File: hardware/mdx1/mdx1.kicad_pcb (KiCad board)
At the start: 4 copper layers, 135 x 92 mm, 322 parts, among them J1 USB-C 16P, J2 USBLC6-2SC6 (USB ESD), J3 Battery JST-PH 3p, J4 Coil header 1x06 2.54mm, J5 SWD 10p 1.27mm, J6 microSD (Hirose DM3AT), J7 UI link FFC 20p 0.5mm, J8 3.5 mm jack, J9 Speaker 8R, Q1 SiR626DP (60V), Q2 BSC190N15NS3 (150V), Q3 BSS127S (600V), Q4 BSC320N20NS3 G, Q5 BSC320N20NS3 G, Q6 BSC320N20NS3 G, Q7 BSC320N20NS3 G, Q8 2N7002, U1 BQ24075RGT, U10 UCC27714D, U11 UCC27714D, U12 INA241A2 (20 V/V), U13 TLV3501 4.5 V (+5 A), U14 TLV3501 0.5 V (-5 A), U15 OPA1612, U16 THS4551 (G=1), U17 THS4551 (G=1), U18 OPA1656, U19 ADS127L01 (ch A), U2 BQ27441-G1A, U20 ADS127L01 (ch B), U21 REF5025 (2.500 V, 3 ppm/C), U22 STM32H743ZIT6, U23 LSM6DSM (IMU), U24 TPA6132A2 (HP amp), U25 PAM8302A (2.5 W class-D), U26 BM83SM1-00AA, U27 MAX-M10S (GNSS), U28 GNSS chip antenna, U3 TPS63001 (3.3V), U4 TPS65131RGE, U5 LT3045 (+5VA), U6 LT3094 (-5VA), U7 TPS7A2033 (+3V3A), U8 LT3757 (VTX 8-30V), U9 LT3757 (VBRIDGE 100V), Y1 16.384 MHz 3225, Y2 32.768 kHz 3215

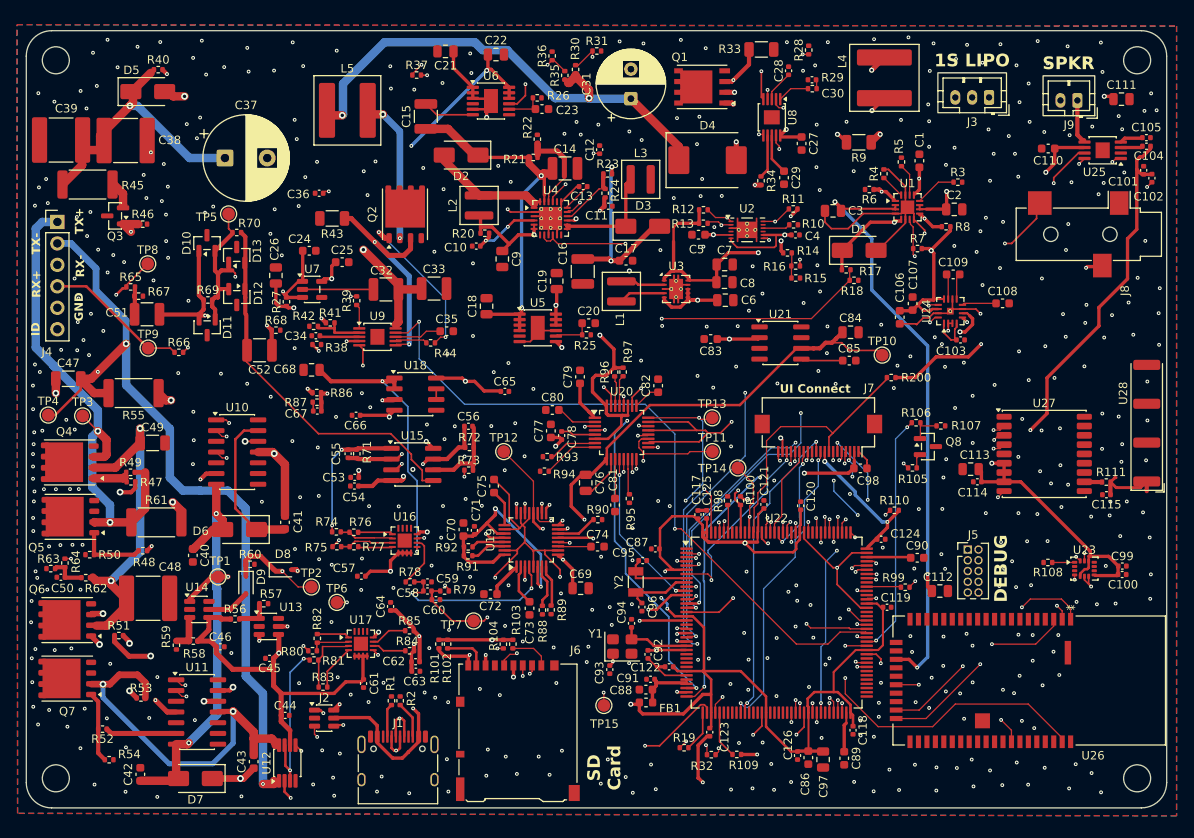
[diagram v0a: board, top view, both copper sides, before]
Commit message: Re-source out-of-stock parts; rework D8/9 footprint and GNSS antenna front end
Parts re-sourced to in-stock equivalents (BOM + board + firmware kept in sync):
- U4  TPS65131RGET, U12 INA241A2QDGKRQ1, U23 LSM6DSO32TR (same footprints)
- Q1  SiR680ADP-T1-UE3 (80 V, same PowerPAK SO-8; higher Qg - verify gate drive)
- U2  BQ27441DRZT-G1A (drop-in, R9 sense retained)
- D8/9 NSVBAT54SWT1G: SOT-323/SC-70 dual-series wired as a single diode
  (anode=pin1, cathode=pin3, pin2 NC); footprint changed on the board
- C32/C33/C38-48 re-sourced (KEMET/Murata/TDK), same footprints

GNSS antenna: chip antenna -> external active antenna via u.FL
- Removed U28 (chip antenna), C115 (match pad), R111 (0R RF series-match)
- Added J13 u.FL (Molex 73412-0110) + bias-tee: L8 27nH feed, C127 33pF DC block,
  C128 10nF VCC_RF bypass, D17 PESD0402-140 ESD (verify Vrwm >= 5 V)

Firmware:
- mdx_config.h: MDX_ITX_V_PER_A 0.4 -> 1.0 (INA241A2 is 50 V/V, not 20)
- hal_stm32.c: LSM6DSO32 accel init 0x48 -> 0x40 (FS_XL encoding differs; keeps +-4 g)
- make test: 96 checks pass

BOM: bom_data.json reconciled to the updated board (every placed part has an MPN;
fab BOM drops only the 15 test points). Regenerated JLCPCB fab package and the
DigiKey upload BOM (grouped by MPN, compact references).
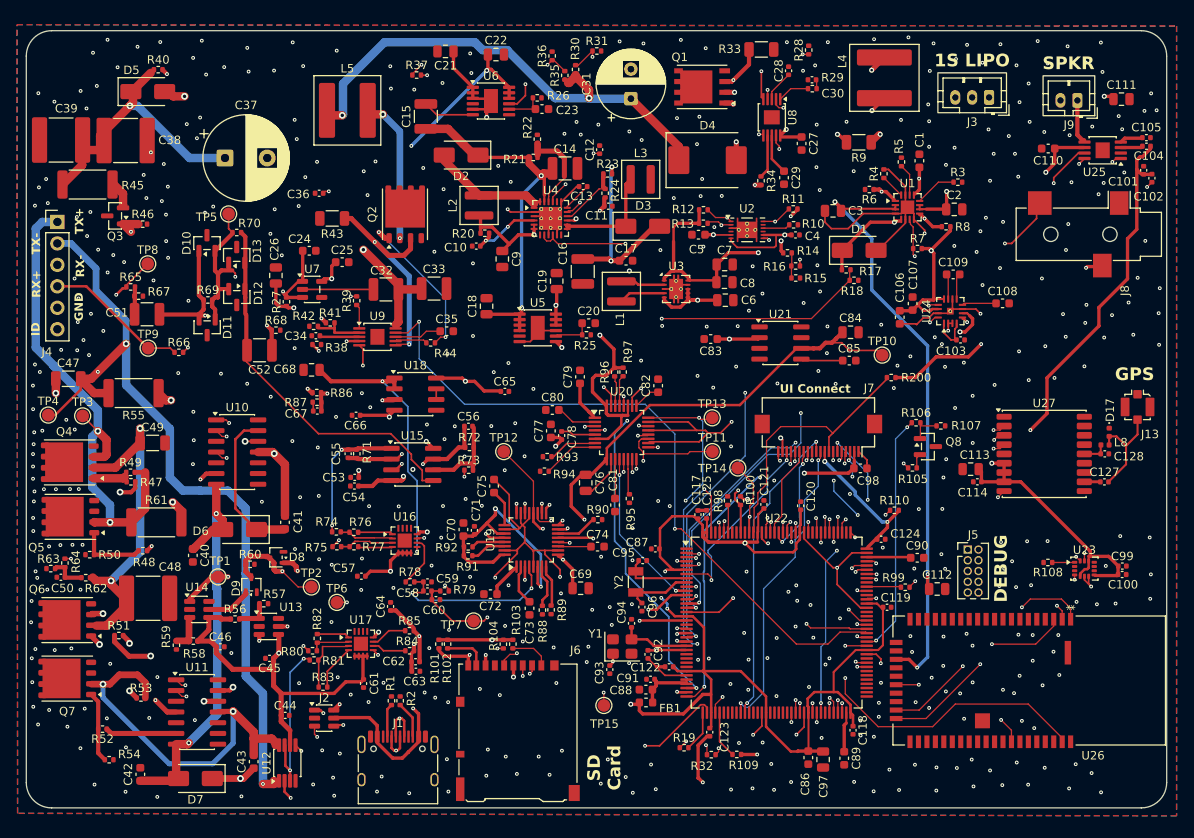
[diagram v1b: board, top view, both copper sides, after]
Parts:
- removed C115: DNP (match, shunt), Capacitor_SMD:C_0402_1005Metric
- removed C126: 100n, Capacitor_SMD:C_0402_1005Metric
- removed H1, H2, H3, H4: MountingHole_3.2mm_M3, MountingHole_3.2mm_M3
- removed R111: 0R (match, series), Resistor_SMD:R_0402_1005Metric
- removed U28: GNSS chip antenna, RF_Antenna:Antenova_SR4G013_GPS
- added C127: 33 pF, Capacitor_SMD:C_0402_1005Metric, F.Cu at (177.6, 103.4)
- added C128: 10nF, Capacitor_SMD:C_0402_1005Metric, F.Cu at (177.7, 100.1)
- added D17: PESD0402-140, Diode_SMD:D_0402_1005Metric, F.Cu at (178.2, 97.5)
- added J13: Conn_Coaxial, Connector_Coaxial:U.FL_Molex_MCRF_73412-0110_Vertical, F.Cu at (181.6, 94.5)
- added L8: 27nH, Inductor_SMD:L_0402_1005Metric, F.Cu at (177.7, 99.0)
- D8, D9: value BAT54WS -> NSVBAT54SWT1G; footprint Diode_SMD:D_SOD-323 -> Package_TO_SOT_SMD:SOT-323_SC-70
- Q1: value SiR626DP (60V) -> SiR680ADP-T1-UE3
- U12: value INA241A2 (20 V/V) -> INA241A2QDGKRQ1
- U2: value BQ27441-G1A -> BQ27441DRZT-G1A
- U23: value LSM6DSM (IMU) -> LSM6DSO32TR
- U4: value TPS65131RGE -> TPS65131RGET
- moved D8 1.67 mm to (79.6, 112.3), turned to 180 degrees
- moved D9 0.63 mm to (76.6, 115.6), turned to 90 degrees
- moved C112 0.40 mm to (157.8, 116.1)
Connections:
- D8 pad 1: TX_FAULT -> /TX driver: 3-level H-bridge, current sense, over-current trip/OC_HI
- D8 pad 2: /TX driver: 3-level H-bridge, current sense, over-current trip/OC_HI -> unconnected-(D8-K-Pad2)
- D9 pad 1: TX_FAULT -> /TX driver: 3-level H-bridge, current sense, over-current trip/OC_LO
- D9 pad 2: /TX driver: 3-level H-bridge, current sense, over-current trip/OC_LO -> unconnected-(D9-K-Pad2)
- U27 pad 11: /UI, audio, wireless: memory LCD, keypad, IMU, headphone + speaker amps, Bluetooth audio, GNSS/GNSS_RF -> Net-(U27-RF_IN)
- U27 pad 14: unconnected-(U27-VCC_RF-Pad14) -> Net-(U27-VCC_RF)
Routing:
- net Net-(D17-A2): track 0.00 -> 12.3 mm
- net /UI, audio, wireless: memory LCD, keypad, IMU, headphone + speaker amps, Bluetooth audio, GNSS/GNSS_ANT: track 6.97 -> 0.00 mm
- net Net-(U27-VCC_RF): track 0.00 -> 3.00 mm
- net /UI, audio, wireless: memory LCD, keypad, IMU, headphone + speaker amps, Bluetooth audio, GNSS/GNSS_RF: track 2.49 -> 0.00 mm
- net Net-(U27-RF_IN): track 0.00 -> 2.33 mm
- net /TX driver: 3-level H-bridge, current sense, over-current trip/OC_HI: track 8.89 -> 10.4 mm
- net TX_FAULT: track 95.4 -> 96.2 mm
- net VBAT: track 95.3 -> 94.5 mm
- net GND: vias 486 -> 461
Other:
- board text added: "GPS"

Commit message: Add LL-audio + expansion-header support (firmware, schematic nets, mount holes)
Firmware (host bench 96/0):
- Optional low-latency audio module (nRF52840 daughterboard on J14): settings
  item "Low-latency audio" + "Pair LL headphones" (auto-exposed to UI and app via
  the item table), settings_t.ll_audio, HAL hal_ll_audio_*(), USART3 (PD8/PD9) +
  PG0/PG1 on the target; BM83 kept for BLE/app + standard-BT audio. Sim stubs.
- Expansion header: I2C4 (PF14/PF15), SPI2 (PB13/14/15, CS PG8), UART5 (PB6/PB12),
  GPIO PE13/PA15 initialised; portable hal_exp_*() API + sim stubs.

Schematic: J14 LL-audio header and expansion-header nets wired to the MCU; cleared
the no-connect flags on the newly used STM32 pins (PD8/9, PG0/1, PF14/15, PB13/14/15,
PG8, PB6, PB12, PE13, PA15).

Board: added 4x M3 (3.2 mm) mounting holes (H1-H4) to the main board at the
enclosure positions (128 x 85 mm rectangle, 3.55 mm inset).

Docs: firmware guide menu, design report (IMU), staged bring-up, and the priced BOM
review updated for the current part set.
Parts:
- added H1: MountingHole_3.2mm_M3, MountingHole_3.2mm_M3, F.Cu at (53.5, 53.5)
- added H2: MountingHole_3.2mm_M3, MountingHole_3.2mm_M3, F.Cu at (53.5, 138.4)
- added H3: MountingHole_3.2mm_M3, MountingHole_3.2mm_M3, F.Cu at (181.4, 53.5)
- added H4: MountingHole_3.2mm_M3, MountingHole_3.2mm_M3, F.Cu at (181.4, 138.4)
- added J14: BT LL Audio (optional), Connector_Samtec_MicroMate:Samtec_T1M-10-X-S-V_1x10-1MP_P1.0mm_Terminal_Vertical, F.Cu at (144.5, 139.7)
- added J15: Expanson Header, Connector_Samtec_MicroMate:Samtec_T1M-12-X-S-V_1x12-1MP_P1.0mm_Terminal_Vertical, F.Cu at (129.8, 139.7)
- moved C97 2.45 mm to (144.2, 133.8)
- moved C89 2.09 mm to (146.5, 134.1)
- moved C86 1.84 mm to (142.7, 134.2)
- moved C4 0.71 mm to (141.8, 74.2)
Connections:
- U22 pad 110: unconnected-(U22-PA15-Pad110) -> EXP_GPIO2
- U22 pad 136: unconnected-(U22-PB6-Pad136) -> EXP_UART_TX
- U22 pad 54: unconnected-(U22-PF14-Pad54) -> EXP_I2C_SCL
- U22 pad 55: unconnected-(U22-PF15-Pad55) -> EXP_I2C_SDA
- U22 pad 56: unconnected-(U22-PG0-Pad56) -> NRF_RESET
- U22 pad 57: unconnected-(U22-PG1-Pad57) -> NRF_STATUS
- U22 pad 66: unconnected-(U22-PE13-Pad66) -> EXP_GPIO1
- U22 pad 73: unconnected-(U22-PB12-Pad73) -> EXP_UART_RX
- U22 pad 74: unconnected-(U22-PB13-Pad74) -> EXP_SPI_SCK
- U22 pad 75: unconnected-(U22-PB14-Pad75) -> EXP_SPI_MISO
- U22 pad 76: unconnected-(U22-PB15-Pad76) -> EXP_SPI_MOSI
- U22 pad 77: unconnected-(U22-PD8-Pad77) -> NRF_RXD
- U22 pad 78: unconnected-(U22-PD9-Pad78) -> NRF_TXD
- U22 pad 93: unconnected-(U22-PG8-Pad93) -> EXP_SPI_CS
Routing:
- net I2S_DOUT: track 50.0 -> 98.3 mm, vias 2 -> 3
- net EXP_GPIO2: track 0.00 -> 46.8 mm, vias 0 -> 5
- net EXP_UART_TX: track 0.00 -> 42.0 mm, vias 0 -> 4
- net EXP_SPI_MOSI: track 0.00 -> 41.8 mm, vias 0 -> 2
- net I2S_LRCLK: track 49.4 -> 88.3 mm, vias 2 -> 3
- net EXP_SPI_CS: track 0.00 -> 35.6 mm, vias 0 -> 2
- net EXP_SPI_MISO: track 0.00 -> 34.7 mm, vias 0 -> 2
- net EXP_GPIO1: track 0.00 -> 33.8 mm, vias 0 -> 2
- net EXP_UART_RX: track 0.00 -> 33.6 mm, vias 0 -> 3
- net EXP_SPI_SCK: track 0.00 -> 31.5 mm, vias 0 -> 2
- net I2S_BCLK: track 51.5 -> 81.6 mm, vias 2 -> 4
- net NRF_RXD: track 0.00 -> 23.3 mm, vias 0 -> 3
- net NRF_TXD: track 0.00 -> 21.7 mm, vias 0 -> 2
- net EXP_I2C_SCL: track 0.00 -> 16.9 mm, vias 0 -> 3
- net EXP_I2C_SDA: track 0.00 -> 16.7 mm, vias 0 -> 2
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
